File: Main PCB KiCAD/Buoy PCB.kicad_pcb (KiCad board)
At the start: 2 copper layers, 100 x 100 mm, 48 parts, among them J1 RS485, J10 Battery, J2 Solar 1, J3 Solar 2, J4 Solar 3, J5 Solar 4, J6 Solar 5, J7 Solar 6, J8 Solar PCB, J9 CAN, U1 MCP2515-xST, U2 TJA1051TK-3, U3 ESP32-S2-WROVER, U4 MAX3072E, U5 BQ24075RGT, U6 BQ27441-G1, Y1 8 MHz

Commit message: battery charging
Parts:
- removed D11, D8: RB550VM-30TE-17, Diode_SMD:D_SOD-323_HandSoldering
- removed J8: Solar PCB, Connector_Molex:Molex_Nano-Fit_105309-xx08_1x08_P2.50mm_Vertical
- removed JP3: Solar - GND, Jumper:SolderJumper-2_P1.3mm_Bridged_RoundedPad1.0x1.5mm
- added C10: 100nF, Capacitor_SMD:C_0805_2012Metric_Pad1.18x1.45mm_HandSolder, F.Cu at (150.6, 95.0)
- added C6: 1u, Capacitor_SMD:C_0805_2012Metric_Pad1.18x1.45mm_HandSolder, F.Cu at (171.2, 133.6)
- added C7: 1uF, Capacitor_SMD:C_0805_2012Metric_Pad1.18x1.45mm_HandSolder, F.Cu at (150.6, 86.0)
- added C8: 1u, Capacitor_SMD:C_0805_2012Metric_Pad1.18x1.45mm_HandSolder, F.Cu at (150.6, 89.0)
- added C9: 1u, Capacitor_SMD:C_0805_2012Metric_Pad1.18x1.45mm_HandSolder, F.Cu at (150.6, 92.0)
- added D12: 1N5819HW-FDICT, Diode_SMD:D_SOD-123, F.Cu at (184.4, 135.1)
- added D13: LED, LED_SMD:LED_0805_2012Metric_Pad1.15x1.40mm_HandSolder, F.Cu at (53.7, 79.1)
- added D14: LED, LED_SMD:LED_0805_2012Metric_Pad1.15x1.40mm_HandSolder, F.Cu at (53.7, 82.2)
- added D15: LED, LED_SMD:LED_0805_2012Metric_Pad1.15x1.40mm_HandSolder, F.Cu at (53.7, 85.2)
- added JP4: LEDs, Jumper:SolderJumper-2_P1.3mm_Bridged_RoundedPad1.0x1.5mm, F.Cu at (48.6, 88.6)
- added Q1: Q_NMOS_DSG, Package_TO_SOT_SMD:SOT-23, F.Cu at (48.9, 80.0)
- added Q2: Q_NMOS_DSG, Package_TO_SOT_SMD:SOT-23, F.Cu at (48.9, 84.6)
- added R11: 1k, Resistor_SMD:R_0805_2012Metric_Pad1.20x1.40mm_HandSolder, F.Cu at (67.1, 31.7)
- added R12: 330, Resistor_SMD:R_0805_2012Metric_Pad1.20x1.40mm_HandSolder, F.Cu at (80.3, 37.3)
- added R13: 330, Resistor_SMD:R_0805_2012Metric_Pad1.20x1.40mm_HandSolder, F.Cu at (80.3, 40.2)
- added R14: 330, Resistor_SMD:R_0805_2012Metric_Pad1.20x1.40mm_HandSolder, F.Cu at (80.3, 43.2)
- added R15: 22k, Resistor_SMD:R_0805_2012Metric_Pad1.20x1.40mm_HandSolder, F.Cu at (67.1, 34.7)
- added R16: 330, Resistor_SMD:R_0805_2012Metric_Pad1.20x1.40mm_HandSolder, F.Cu at (67.1, 37.6)
- added R17: 22k, Resistor_SMD:R_0805_2012Metric_Pad1.20x1.40mm_HandSolder, F.Cu at (67.1, 40.6)
- added R18: 22k, Resistor_SMD:R_0805_2012Metric_Pad1.20x1.40mm_HandSolder, F.Cu at (67.1, 43.5)
- added R19: 2.7k, Resistor_SMD:R_0805_2012Metric_Pad1.20x1.40mm_HandSolder, F.Cu at (67.1, 46.5)
- D10, D3, D4, D5, D6, D7: value RB550VM-30TE-17 -> 1N5819HW-FDICT; footprint Diode_SMD:D_SOD-323_HandSoldering -> Diode_SMD:D_SOD-123
- J10: value Battery -> USB_B_Micro; footprint Connector_Molex:Molex_Nano-Fit_105309-xx02_1x02_P2.50mm_Vertical -> Connector_USB:USB_Micro-B_Amphenol_10103594-0001LF_Horizontal
- R4: value 1k -> 330
- R5, R6, R8, R9: value 1k -> 10k
- U5: value BQ24075RGT -> AP7215-33YG-13
- U6: value BQ27441-G1 -> MCP73834T-FCI/UN
- moved J10 136.8 mm to (187.5, 141.4)
- moved U6 121.7 mm to (177.3, 133.6)
- moved D10 121.6 mm to (184.4, 132.6)
- moved U5 106.2 mm to (169.1, 126.7)
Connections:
- C1 pad 2: -Batt -> GND
- C2 pad 2: -Batt -> GND
- C3 pad 2: -Batt -> GND
- C4 pad 2: -Batt -> GND
- C5 pad 2: -Batt -> GND
- D1 pad 1: -Batt -> GND
- D10 pad 1: Net-(D10-K) -> +Solar
- D10 pad 2: +Solar -> Net-(D10-A)
- D2 pad 1: -Batt -> GND
- D9 pad 1: -Solar -> GND
- J1 pad 4: -Batt -> GND
- J1 pad 8: -Batt -> GND
- J10 pad 1: +Batt -> Net-(D12-A)
- J10 pad 2: -Batt -> unconnected-(J10-D--Pad2)
- J2 pad 1: Net-(D3-A) -> Net-(D10-A)
- J2 pad 2: -Solar -> GND
- J3 pad 1: Net-(D4-A) -> Net-(D3-A)
- J3 pad 2: -Solar -> GND
- J4 pad 1: Net-(D5-A) -> Net-(D4-A)
- J4 pad 2: -Solar -> GND
- J5 pad 1: Net-(D6-A) -> Net-(D7-A)
- J5 pad 2: -Solar -> GND
- J6 pad 1: Net-(D7-A) -> Net-(D6-A)
- J6 pad 2: -Solar -> GND
- J7 pad 1: Net-(D8-A) -> Net-(D5-A)
- J7 pad 2: -Solar -> GND
- J9 pad 4: -Batt -> GND
- J9 pad 8: -Batt -> GND
- R4 pad 1: +5V -> +3.3V
- R9 pad 2: -Solar -> GND
- U1 pad 10: -Batt -> GND
- U2 pad 2: -Batt -> GND
- U2 pad 8: -Batt -> GND
- U2 pad 9: -Batt -> GND
- U3 pad 1: -Batt -> GND
- U3 pad 2: unconnected-(U3-3V3-Pad2) -> +3.3V
- U3 pad 26: -Batt -> GND
- U3 pad 42: -Batt -> GND
- U3 pad 43: -Batt -> GND
- U4 pad 5: -Batt -> GND
- U5 pad 1: unconnected-(U5-TS-Pad1) -> GND
- U5 pad 10: +5V -> (no net)
- U5 pad 11: +5V -> (no net)
- U5 pad 12: unconnected-(U5-ILIM-Pad12) -> (no net)
- U5 pad 13: unconnected-(U5-IN-Pad13) -> (no net)
- U5 pad 14: unconnected-(U5-TMR-Pad14) -> (no net)
- U5 pad 15: unconnected-(U5-SYSOFF-Pad15) -> (no net)
- U5 pad 16: unconnected-(U5-ISET-Pad16) -> (no net)
- U5 pad 17: Net-(U5-VSS-Pad17) -> (no net)
- U5 pad 3: +Batt -> +3.3V
- U5 pad 4: unconnected-(U5-~{CE}-Pad4) -> (no net)
- U5 pad 5: unconnected-(U5-EN2-Pad5) -> (no net)
- U5 pad 6: unconnected-(U5-EN1-Pad6) -> (no net)
- U5 pad 7: unconnected-(U5-~{PGOOD}-Pad7) -> (no net)
- U5 pad 8: Net-(U5-VSS-Pad17) -> (no net)
- U5 pad 9: unconnected-(U5-~{CHG}-Pad9) -> (no net)
- U6 pad 1: unconnected-(U6-SDA-Pad1) -> +Solar
- U6 pad 10: unconnected-(U6-BIN-Pad10) -> +Batt
- U6 pad 11: unconnected-(U6-NC-Pad11) -> (no net)
- U6 pad 12: unconnected-(U6-GPOUT-Pad12) -> (no net)
- U6 pad 13: unconnected-(U6-PAD-Pad13) -> (no net)
- U6 pad 2: unconnected-(U6-SCL-Pad2) -> +Solar
- U6 pad 3: unconnected-(U6-V_{SS}-Pad3) -> /Battery Charger/Status1
- U6 pad 4: unconnected-(U6-NC-Pad4) -> /Battery Charger/Status2
- U6 pad 5: unconnected-(U6-V_{DD}-Pad5) -> GND
- U6 pad 6: unconnected-(U6-BAT-Pad6) -> Net-(U6-PROG)
- U6 pad 7: unconnected-(U6-SRN-Pad7) -> /Battery Charger/PG
- U6 pad 8: unconnected-(U6-SRP-Pad8) -> Net-(U6-THERM)
- U6 pad 9: unconnected-(U6-NC-Pad9) -> +Batt
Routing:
- net GND: track 0.00 -> 78.3 mm, vias 0 -> 1
- net -Solar: track 78.3 -> 0.00 mm, vias 1 -> 0
- net +5V: track 6.70 -> 0.00 mm, vias 1 -> 0
- net -Batt: track 11.4 -> 5.54 mm
- net Net-(D8-A): track 3.34 -> 0.00 mm
- net Net-(D5-A): track 4.55 -> 7.89 mm
- net +Solar: track 43.6 -> 42.1 mm

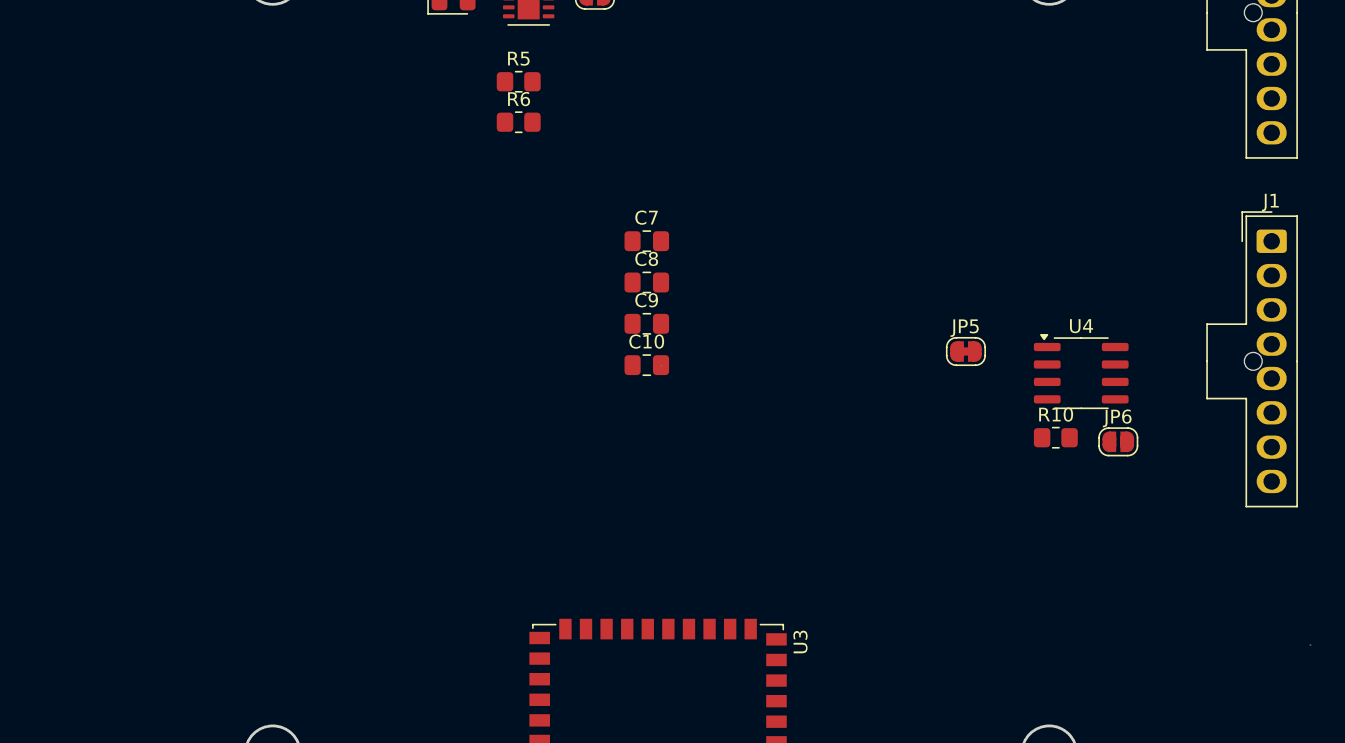
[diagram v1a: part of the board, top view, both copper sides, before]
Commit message: updated 18650
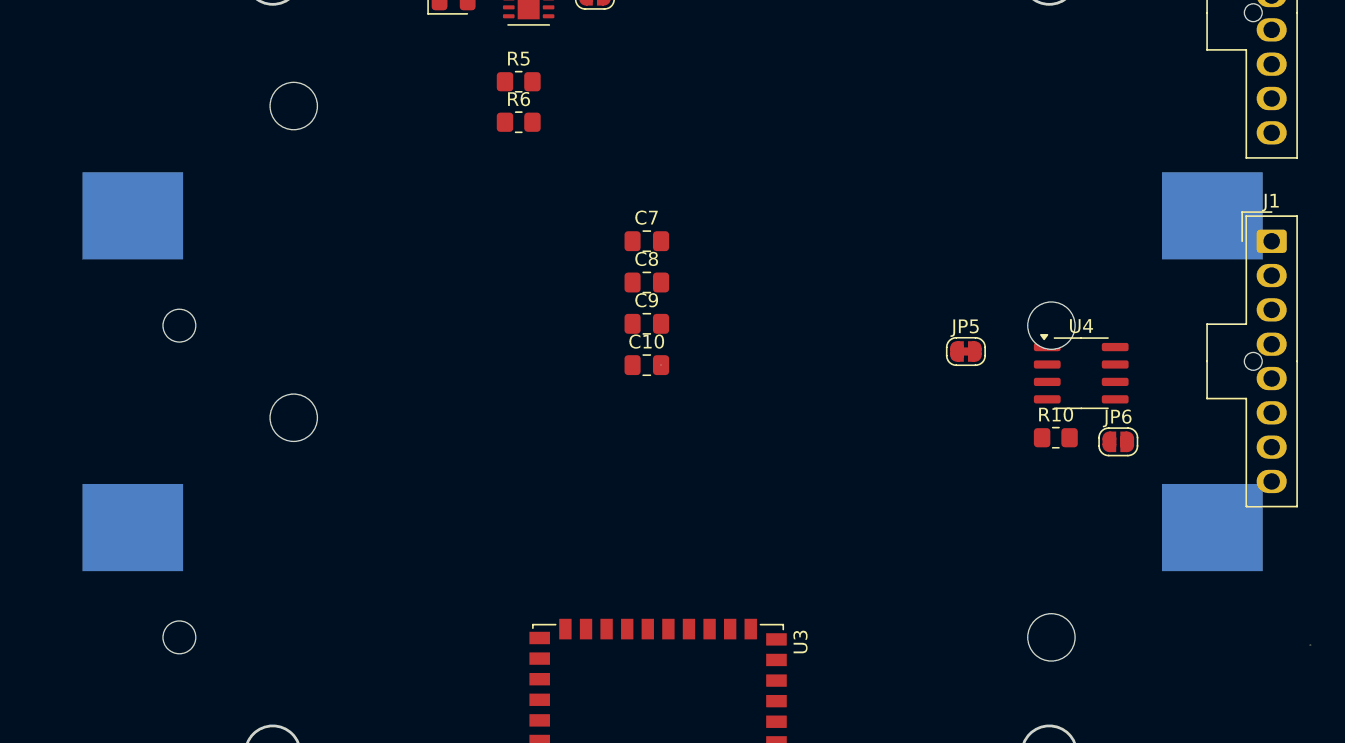
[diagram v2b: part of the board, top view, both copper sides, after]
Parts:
- added BT1: 18650, Batteries:18650 Holder, B.Cu at (152.4, 84.1)
- added BT2: 18650, Batteries:18650 Holder, B.Cu at (152.4, 106.8)

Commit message: this is likely to break all the things…
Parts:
- removed C1, C2: 0.1uF, Capacitor_SMD:C_0805_2012Metric_Pad1.18x1.45mm_HandSolder
- removed C10: 100nF, Capacitor_SMD:C_0805_2012Metric_Pad1.18x1.45mm_HandSolder
- removed C3: 10uF, Capacitor_SMD:C_0805_2012Metric_Pad1.18x1.45mm_HandSolder
- removed C4, C5: 22pF, Capacitor_SMD:C_0805_2012Metric_Pad1.18x1.45mm_HandSolder
- removed C7: 1uF, Capacitor_SMD:C_0805_2012Metric_Pad1.18x1.45mm_HandSolder
- removed C8, C9: 1u, Capacitor_SMD:C_0805_2012Metric_Pad1.18x1.45mm_HandSolder
- removed D1: RED, LED_SMD:LED_0805_2012Metric_Pad1.15x1.40mm_HandSolder
- removed D14, D15: LED, LED_SMD:LED_0805_2012Metric_Pad1.15x1.40mm_HandSolder
- removed J2: Solar 1, Connector_Molex:Molex_Nano-Fit_105309-xx02_1x02_P2.50mm_Vertical
- removed J3: Solar 2, Connector_Molex:Molex_Nano-Fit_105309-xx02_1x02_P2.50mm_Vertical
- removed J4: Solar 3, Connector_Molex:Molex_Nano-Fit_105309-xx02_1x02_P2.50mm_Vertical
- removed J5: Solar 4, Connector_Molex:Molex_Nano-Fit_105309-xx02_1x02_P2.50mm_Vertical
- removed J6: Solar 5, Connector_Molex:Molex_Nano-Fit_105309-xx02_1x02_P2.50mm_Vertical
- removed J7: Solar 6, Connector_Molex:Molex_Nano-Fit_105309-xx02_1x02_P2.50mm_Vertical
- removed JP1: RS485 - Power, Jumper:SolderJumper-2_P1.3mm_Bridged_RoundedPad1.0x1.5mm
- removed JP2, JP6: Terminator, Jumper:SolderJumper-2_P1.3mm_Open_RoundedPad1.0x1.5mm
- removed JP4: LEDs, Jumper:SolderJumper-2_P1.3mm_Bridged_RoundedPad1.0x1.5mm
- removed JP5: CAN - Power, Jumper:SolderJumper-2_P1.3mm_Bridged_RoundedPad1.0x1.5mm
- removed Q1, Q2: Q_NMOS_DSG, Package_TO_SOT_SMD:SOT-23
- removed R1, R11: 1k, Resistor_SMD:R_0805_2012Metric_Pad1.20x1.40mm_HandSolder
- removed R10, R3: 120, Resistor_SMD:R_0805_2012Metric_Pad1.20x1.40mm_HandSolder
- removed R12, R13, R14, R16: 330, Resistor_SMD:R_0805_2012Metric_Pad1.20x1.40mm_HandSolder
- removed R15, R17, R18: 22k, Resistor_SMD:R_0805_2012Metric_Pad1.20x1.40mm_HandSolder
- removed R19: 2.7k, Resistor_SMD:R_0805_2012Metric_Pad1.20x1.40mm_HandSolder
- removed R2: 10k, Resistor_SMD:R_0805_2012Metric_Pad1.20x1.40mm_HandSolder
- removed U1: MCP2515-xST, Package_SO:TSSOP-20_4.4x6.5mm_P0.65mm
- removed U2: TJA1051TK-3, Package_SON:HVSON-8-1EP_3x3mm_P0.65mm_EP1.6x2.4mm
- removed U4: MAX3072E, Package_SO:SOIC-8_3.9x4.9mm_P1.27mm
- removed U5: AP7215-33YG-13, Package_DFN_QFN:VQFN-16-1EP_3x3mm_P0.5mm_EP1.6x1.6mm
- removed U6: MCP73834T-FCI/UN, Package_SON:Texas_S-PDSO-N12
- removed Y1: 8 MHz, Crystal:Crystal_SMD_0603-2Pin_6.0x3.5mm_HandSoldering
- added J8: Solar, Connector_Molex:Molex_Nano-Fit_105309-xx08_1x08_P2.50mm_Vertical, F.Cu at (120.7, 115.8)
- D9, R4: moved to F.Cu
- moved D13 125.3 mm to (172.7, 40.0)
- moved J10 105.4 mm to (157.0, 40.5), turned to 180 degrees
- moved R7 93.9 mm to (168.3, 42.5)
- moved D12 92.7 mm to (160.0, 45.7), turned to 180 degrees
- moved D2 92.2 mm to (163.8, 40.0)
- moved D9 91.4 mm to (168.3, 40.0), turned to 0 degrees
- moved R4 87.4 mm to (163.8, 42.5), turned to 0 degrees
- moved D6 76.7 mm to (127.0, 125.1)
- moved C6 75.3 mm to (151.1, 61.0)
- moved D7 74.2 mm to (127.0, 116.8)
- moved R8 72.6 mm to (132.1, 75.6), turned to 0 degrees
- moved R9 72.4 mm to (135.9, 75.6)
- moved U3 72.4 mm to (127.9, 57.3), turned to 0 degrees
- moved D10 60.2 mm to (127.0, 114.3), turned to 180 degrees
- moved D3 49.1 mm to (127.0, 132.7), turned to 180 degrees
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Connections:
- D2 pad 1: GND -> Net-(D2-K)
- D2 pad 2: Net-(D2-A) -> +3.3V
- D9 pad 1: GND -> Net-(D9-K)
- D9 pad 2: Net-(D9-A) -> +Solar
- R4 pad 1: +3.3V -> Net-(D2-K)
- R4 pad 2: Net-(D2-A) -> GND
- R7 pad 1: +Solar -> Net-(D9-K)
- R7 pad 2: Net-(D9-A) -> GND
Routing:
- net GND: track 78.3 -> 2.50 mm, vias 1 -> 0
- net +Solar: track 42.1 -> 19.0 mm
- net -Batt: track 5.54 -> 0.00 mm
- net Net-(D10-A): track 0.00 -> 5.34 mm
- net /Solar/V_Solar_An: track 4.89 -> 0.00 mm
- net Net-(D6-A): track 3.34 -> 6.46 mm
- net Net-(D3-A): track 4.04 -> 6.51 mm
- net Net-(D4-A): track 4.34 -> 6.49 mm
- net Net-(D9-A): track 2.04 -> 0.00 mm, vias 1 -> 0
- net Net-(D2-A): track 2.02 -> 0.00 mm, vias 1 -> 0
- net Net-(D7-A): track 3.34 -> 5.33 mm
- net Net-(D5-A): track 7.89 -> 6.47 mm
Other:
- board size 100 x 100 mm -> 78.5 x 108.2 mm

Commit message: clean
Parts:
- removed D10: 1N5819HW-FDICT, Diode_SMD:D_SOD-123
- added C10: 100nF, Capacitor_SMD:C_0805_2012Metric_Pad1.18x1.45mm_HandSolder, F.Cu at (156.2, 119.4)
- added C7: 1uF, Capacitor_SMD:C_0805_2012Metric_Pad1.18x1.45mm_HandSolder, F.Cu at (115.6, 30.5)
- added C8: 1u, Capacitor_SMD:C_0805_2012Metric_Pad1.18x1.45mm_HandSolder, F.Cu at (202.2, 80.8)
- added C9: 1u, Capacitor_SMD:C_0805_2012Metric_Pad1.18x1.45mm_HandSolder, F.Cu at (202.2, 83.8)
- added D1: 1N5819HW-FDICT, Diode_SMD:D_SOD-123, F.Cu at (166.4, 43.2)
- added D14: LED, LED_SMD:LED_0805_2012Metric_Pad1.15x1.40mm_HandSolder, F.Cu at (165.1, 36.8)
- added D15: LED, LED_SMD:LED_0805_2012Metric_Pad1.15x1.40mm_HandSolder, F.Cu at (161.3, 36.8)
- added J11: Conn_01x12_Socket, Connector_PinSocket_2.54mm:PinSocket_1x12_P2.54mm_Vertical, B.Cu at (172.7, 43.2)
- added JP1: RS485 - Power, Jumper:SolderJumper-2_P1.3mm_Bridged_RoundedPad1.0x1.5mm, F.Cu at (43.0, 69.3)
- added JP4: LEDs, Jumper:SolderJumper-2_P1.3mm_Bridged_RoundedPad1.0x1.5mm, F.Cu at (161.3, 43.2)
- added JP6: Terminator, Jumper:SolderJumper-2_P1.3mm_Open_RoundedPad1.0x1.5mm, F.Cu at (43.0, 72.8)
- added Q1: Q_NMOS_DSG, Package_TO_SOT_SMD:SOT-23, F.Cu at (156.2, 123.5)
- added Q2: Q_NMOS_DSG, Package_TO_SOT_SMD:SOT-23, F.Cu at (161.3, 123.5)
- added R10: 120, Resistor_SMD:R_0805_2012Metric_Pad1.20x1.40mm_HandSolder, F.Cu at (43.2, 76.1)
- added R11: 1k, Resistor_SMD:R_0805_2012Metric_Pad1.20x1.40mm_HandSolder, F.Cu at (192.6, 80.7)
- added R12: 330, Resistor_SMD:R_0805_2012Metric_Pad1.20x1.40mm_HandSolder, F.Cu at (168.9, 39.4)
- added R13: 330, Resistor_SMD:R_0805_2012Metric_Pad1.20x1.40mm_HandSolder, F.Cu at (165.1, 39.4)
- added R14: 330, Resistor_SMD:R_0805_2012Metric_Pad1.20x1.40mm_HandSolder, F.Cu at (161.3, 39.4)
- added R15: 22k, Resistor_SMD:R_0805_2012Metric_Pad1.20x1.40mm_HandSolder, F.Cu at (157.5, 43.2)
- added R16: 330, Resistor_SMD:R_0805_2012Metric_Pad1.20x1.40mm_HandSolder, F.Cu at (156.2, 116.8)
- added R17: 22k, Resistor_SMD:R_0805_2012Metric_Pad1.20x1.40mm_HandSolder, F.Cu at (154.9, 43.2)
- added R18: 22k, Resistor_SMD:R_0805_2012Metric_Pad1.20x1.40mm_HandSolder, F.Cu at (152.4, 43.2)
- added R19: 2.7k, Resistor_SMD:R_0805_2012Metric_Pad1.20x1.40mm_HandSolder, F.Cu at (161.3, 118.1)
- added U4: MAX3072E, Package_SO:SOIC-8_3.9x4.9mm_P1.27mm, F.Cu at (45.1, 64.3)
- BT1, BT2: footprint Batteries:18650 Holder -> Battery:BatteryHolder_Keystone_1042_1x18650
- J8: value Solar -> Conn_01x12_Pin; footprint Connector_Molex:Molex_Nano-Fit_105309-xx08_1x08_P2.50mm_Vertical -> Connector_PinHeader_2.54mm:PinHeader_1x12_P2.54mm_Vertical
- J9: value CAN -> Conn_01x12_Socket; footprint Connector_Molex:Molex_Nano-Fit_105309-xx08_1x08_P2.50mm_Vertical -> Connector_PinSocket_2.54mm:PinSocket_1x12_P2.54mm_Vertical
- U3: moved to B.Cu
- moved D2 145.4 mm to (18.7, 49.4)
- moved R4 140.6 mm to (23.4, 49.4)
- moved J1 137.5 mm to (38.1, 63.7)
- moved D3 95.5 mm to (166.4, 45.7), turned to 0 degrees
- moved D4 90.9 mm to (166.4, 48.3), turned to 0 degrees
- moved D5 86.3 mm to (166.4, 50.8), turned to 0 degrees
- moved D6 81.8 mm to (166.4, 53.3), turned to 0 degrees
- moved J8 72.7 mm to (119.4, 43.2)
- moved D7 72.6 mm to (166.4, 55.9), turned to 0 degrees
- moved J9 67.6 mm to (108.0, 43.2)
- moved D12 65.6 mm to (104.1, 80.0), turned to -90 degrees
- moved J10 61.6 mm to (109.7, 80.0), turned to 90 degrees
- moved C6 54.2 mm to (116.8, 19.1), turned to 0 degrees
- moved U3 46.5 mm to (81.5, 53.5), turned to 180 degrees
- moved R5 41.8 mm to (161.3, 48.3), turned to -90 degrees
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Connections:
- C6 pad 1: +Solar -> +Solar_Batt
- C6 pad 2: GND -> GND_Batt
- D2 pad 1: Net-(D2-K) -> GND
- D2 pad 2: +3.3V -> Net-(D2-A)
- D3 pad 1: +Solar -> +Solar_Batt
- D4 pad 1: +Solar -> +Solar_Batt
- D5 pad 1: +Solar -> +Solar_Batt
- D6 pad 1: +Solar -> +Solar_Batt
- D7 pad 1: +Solar -> +Solar_Batt
- D9 pad 1: Net-(D9-K) -> GND_Batt
- D9 pad 2: +Solar -> Net-(D9-A)
- J8 pad 1: Net-(D10-A) -> +3.3V_bat
- J8 pad 2: Net-(D7-A) -> +Solar_Batt
- J8 pad 3: Net-(D6-A) -> GND_Batt
- J8 pad 4: Net-(D5-A) -> GND_Batt
- J8 pad 5: Net-(D4-A) -> /V_Batt_An
- J8 pad 6: Net-(D3-A) -> /V_Solar_An
- J8 pad 7: GND -> GND_Batt
- J8 pad 8: GND -> unconnected-(J8-Pin_8-Pad8)
- J9 pad 1: Net-(J9-Pin_1) -> +3.3V
- J9 pad 2: /CAN Interface/CAN_H -> +Solar
- J9 pad 3: /CAN Interface/CAN_L -> GND
- J9 pad 5: Net-(J9-Pin_1) -> unconnected-(J9-Pin_5-Pad5)
- J9 pad 6: /CAN Interface/CAN_H -> unconnected-(J9-Pin_6-Pad6)
- J9 pad 7: /CAN Interface/CAN_L -> GND
- J9 pad 8: GND -> unconnected-(J9-Pin_8-Pad8)
- R4 pad 1: Net-(D2-K) -> +3.3V
- R4 pad 2: GND -> Net-(D2-A)
- R5 pad 2: /Battery Charger/V_Batt_An -> /V_Batt_An
- R6 pad 1: /Battery Charger/V_Batt_An -> /V_Batt_An
- R7 pad 1: Net-(D9-K) -> +Solar_Batt
- R7 pad 2: GND -> Net-(D9-A)
- R8 pad 1: +Solar -> +Solar_Batt
- R8 pad 2: /Solar/V_Solar_An -> /V_Solar_An
- R9 pad 1: /Solar/V_Solar_An -> /V_Solar_An
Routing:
- net -Batt: track 0.00 -> 111.2 mm, vias 0 -> 2
- net +Batt: track 0.00 -> 95.0 mm, vias 0 -> 2
- net +Solar_Batt: track 0.00 -> 73.5 mm
- net +3.3V_bat: track 0.00 -> 38.5 mm
- net Net-(D13-A): track 0.00 -> 25.2 mm
- net +Solar: track 19.0 -> 38.6 mm
- net /Battery Charger/Status2: track 0.00 -> 13.3 mm
- net /Battery Charger/Status1: track 0.00 -> 11.5 mm
- net Net-(D7-A): track 5.33 -> 14.6 mm
- net /Battery Charger/PG: track 0.00 -> 9.05 mm
- net GND_Batt: track 0.00 -> 6.50 mm
- net Net-(D6-A): track 6.46 -> 12.1 mm
- net Net-(D10-A): track 5.34 -> 0.00 mm
- net Net-(D1-A): track 0.00 -> 4.70 mm
- net Net-(D12-A): track 0.00 -> 3.94 mm
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- added copper zone on F.Cu, net GND
- added copper zone on F.Cu, net GND_Batt
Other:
- board size 78.5 x 108.2 mm -> 123.5 x 100 mm
- board text added: "0"
- board text added: "0 mm"
- board text added: "0.01 mm"
- board text added: "0.02"
- board text added: "0.035 mm"
- board text added: "1"
- board text added: "1.51 mm"
- board text added: "3.3"
- board text added: "4.5"
- board text added: "B.Cu"
- board text added: "B.Mask"
- board text added: "B.Paste"
- board text added: "B.Silkscreen"
- board text added: "Bottom Silk Screen"
- board text added: "Bottom Solder Mask"
- board text added: "Bottom Solder Paste"
- board text added: "Color"
- board text added: "Dielectric"
- board text added: "Epsilon R"
- board text added: "F.Cu"
- board text added: "F.Mask"
- board text added: "F.Paste"
- board text added: "F.Silkscreen"
- board text added: "FR4"
- board text added: "Layer Name"
- board text added: "Loss Tangent"
- board text added: "Material"
- board text added: "Not specified"
- board text added: "Thickness (mm)"
- board text added: "Top Silk Screen"
- board text added: "Top Solder Mask"
- board text added: "Top Solder Paste"
- board text added: "Type"
- board text added: "copper"
- board text added: "core"

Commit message: update
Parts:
- added J2: Conn_01x12_Socket, Connector_PinSocket_2.54mm:PinSocket_1x12_P2.54mm_Vertical, F.Cu at (54.9, 43.2)
- added J3: Conn_01x12_Pin, Connector_PinHeader_2.54mm:PinHeader_1x12_P2.54mm_Vertical, F.Cu at (172.7, 43.2)
- D13, D14, D15: value LED -> RED
- moved JP4 97.2 mm to (228.2, 113.7)
- moved R15 97.2 mm to (224.4, 113.7)
- moved R17 97.2 mm to (221.9, 113.7)
- moved R5 97.2 mm to (228.2, 118.8)
- moved R6 97.2 mm to (228.2, 122.6)
- moved R18 97.2 mm to (219.3, 113.7)
- moved R8 97.2 mm to (223.2, 118.8)
- moved R9 97.2 mm to (223.2, 122.6)
- moved J11 89.2 mm to (161.0, 131.6), turned to 90 degrees
- moved D1 85.0 mm to (148.8, 126.4), turned to -90 degrees
- moved D3 83.1 mm to (146.3, 126.4), turned to -90 degrees
- moved D4 81.3 mm to (143.8, 126.4), turned to -90 degrees
- moved D5 79.6 mm to (141.2, 126.4), turned to -90 degrees
- moved D6 78.1 mm to (138.7, 126.4), turned to -90 degrees
- moved D7 76.7 mm to (136.1, 126.4), turned to -90 degrees
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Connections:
- R9 pad 2: GND -> GND_Batt
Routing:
- net -Batt: track 111.2 -> 9.06 mm, vias 2 -> 1
- net +Batt: track 95.0 -> 7.04 mm
- net +Solar_Batt: track 73.5 -> 14.8 mm
- net +3.3V_bat: track 38.5 -> 5.08 mm
- net Net-(D13-A): track 25.2 -> 11.4 mm
- net /Battery Charger/Status2: track 13.3 -> 0.00 mm
- net /Battery Charger/Status1: track 11.5 -> 0.00 mm
- net Net-(D7-A): track 14.6 -> 3.77 mm
- net /Battery Charger/PG: track 9.05 -> 0.00 mm
- net Net-(D1-A): track 4.70 -> 13.7 mm
- net Net-(D6-A): track 12.1 -> 4.40 mm
- net Net-(D3-A): track 5.75 -> 11.1 mm
- net unconnected-(J3-Pin_11-Pad11): track 0.00 -> 4.16 mm
- net unconnected-(J3-Pin_7-Pad7): track 0.00 -> 3.97 mm
- net Net-(D5-A): track 9.57 -> 6.04 mm
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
